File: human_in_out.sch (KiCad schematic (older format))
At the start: 47 parts

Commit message: add more buttons
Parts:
- removed R?: R, symbol Device:R
- removed SW? (x2): SW_Push_45deg, symbol Switch:SW_Push_45deg
- removed U? (x7): 74HC04, symbol 74xx:74HC04
- added C?: 100n, symbol Device:C
- added C? (x8): 330n, symbol Device:C
- added R? (x7): 10k, symbol Device:R
- added SW? (x8): SW_Push, symbol Switch:SW_Push
- added U? (x14): 74HC14, symbol 74xx:74HC14
- R?: value R -> 10k
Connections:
- net labels added: BTN3, BTN4, BTN5, BTN6, BTN7, BTN8
- wire segments 58 -> 99
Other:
- moved on the sheet: C?, R?, SW?

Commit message: Finish LED branches on programmer sheet
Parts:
- added D? (x2): LED, symbol Device:LED
- added R? (x2): R, symbol Device:R
- added U? (x2): 74HC14, symbol 74xx:74HC14
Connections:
- net +3V3: now also R?.1, R?.1
- new net: D?.1 (K), U?.8
- new net: D?.1 (K), U?.12
- new net: D?.2 (A), R?.2 (x2)
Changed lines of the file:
@@
 Wire Wire Line
 	4850 1450 6200 1450
-Wire Bus Line
-	4550 4750 4550 5900
-Wire Bus Line
-	6300 900  6300 4750
 Text Label 5950 1450 0    50   ~ 0
 BTN1
@@
 Text Label 6000 2850 0    50   ~ 0
 BTN8
+$Comp
+L Device:LED D?
+U 1 1 60ACE318
+P 8400 5250
+F 0 "D?" V 8439 5132 50  0000 R CNN
+F 1 "LED" V 8348 5132 50  0000 R CNN
+F 2 "" H 8400 5250 50  0001 C CNN
+F 3 "~" H 8400 5250 50  0001 C CNN
+	1    8400 5250
+	0    -1   -1   0
+$EndComp
+$Comp
+L Device:R R?
+U 1 1 60ACF032
+P 8400 4950
+F 0 "R?" H 8470 4996 50  0000 L CNN
+F 1 "R" H 8470 4905 50  0000 L CNN
+F 2 "" V 8330 4950 50  0001 C CNN
+F 3 "~" H 8400 4950 50  0001 C CNN
+	1    8400 4950
+	1    0    0    -1
+$EndComp
+$Comp
+L Device:LED D?
+U 1 1 60ACF03C
+P 8800 5250
+F 0 "D?" V 8839 5132 50  0000 R CNN
+F 1 "LED" V 8748 5132 50  0000 R CNN
+F 2 "" H 8800 5250 50  0001 C CNN
+F 3 "~" H 8800 5250 50  0001 C CNN
+	1    8800 5250
+	0    -1   -1   0
+$EndComp
+$Comp
+L Device:R R?
+U 1 1 60ACF046
+P 8800 4950
+F 0 "R?" H 8870 4996 50  0000 L CNN
+F 1 "R" H 8870 4905 50  0000 L CNN
+F 2 "" V 8730 4950 50  0001 C CNN
+F 3 "~" H 8800 4950 50  0001 C CNN
+	1    8800 4950
+	1    0    0    -1
+$EndComp
+$Comp
+L power:+3.3V #PWR?
+U 1 1 60ACF050
+P 8400 4800
+F 0 "#PWR?" H 8400 4650 50  0001 C CNN
+F 1 "+3.3V" H 8415 4973 50  0000 C CNN
+F 2 "" H 8400 4800 50  0001 C CNN
+F 3 "" H 8400 4800 50  0001 C CNN
+	1    8400 4800
+	1    0    0    -1
+$EndComp
+$Comp
+L power:+3.3V #PWR?
+U 1 1 60ACF05A
+P 8800 4800
+F 0 "#PWR?" H 8800 4650 50  0001 C CNN
+F 1 "+3.3V" H 8815 4973 50  0000 C CNN
+F 2 "" H 8800 4800 50  0001 C CNN
+F 3 "" H 8800 4800 50  0001 C CNN
+	1    8800 4800
+	1    0    0    -1
+$EndComp
+$Comp
+L 74xx:74HC14 U?
+U 6 1 60AC6636
+P 8000 6050
+F 0 "U?" H 8000 6367 50  0000 C CNN
+F 1 "74HC14" H 8000 6276 50  0000 C CNN
+F 2 "" H 8000 6050 50  0001 C CNN
+F 3 "http://www.ti.com/lit/gpn/sn74HC14" H 8000 6050 50  0001 C CNN
+	6    8000 6050
+	1    0    0    -1
+$EndComp
+$Comp
+L 74xx:74HC14 U?
+U 4 1 60AC6630
+P 8000 5500
+AR Path="/6005349A/60AC6630" Ref="U?"  Part="4"
+AR Path="/608DD7ED/60AC6630" Ref="U?"  Part="4"
+F 0 "U?" H 8000 5817 50  0000 C CNN
+F 1 "74HC14" H 8000 5726 50  0000 C CNN
+F 2 "" H 8000 5500 50  0001 C CNN
+F 3 "http://www.ti.com/lit/gpn/sn74HC14" H 8000 5500 50  0001 C CNN
+	4    8000 5500
+	1    0    0    -1
+$EndComp
+Wire Wire Line
+	8300 5500 8400 5500
+Wire Wire Line
+	8400 5500 8400 5400
+Wire Wire Line
+	8300 6050 8800 6050
+Wire Wire Line
+	8800 6050 8800 5400
+Wire Bus Line
+	4550 4750 4550 5900
+Wire Bus Line
+	6300 900  6300 4750
 $EndSCHEMATC

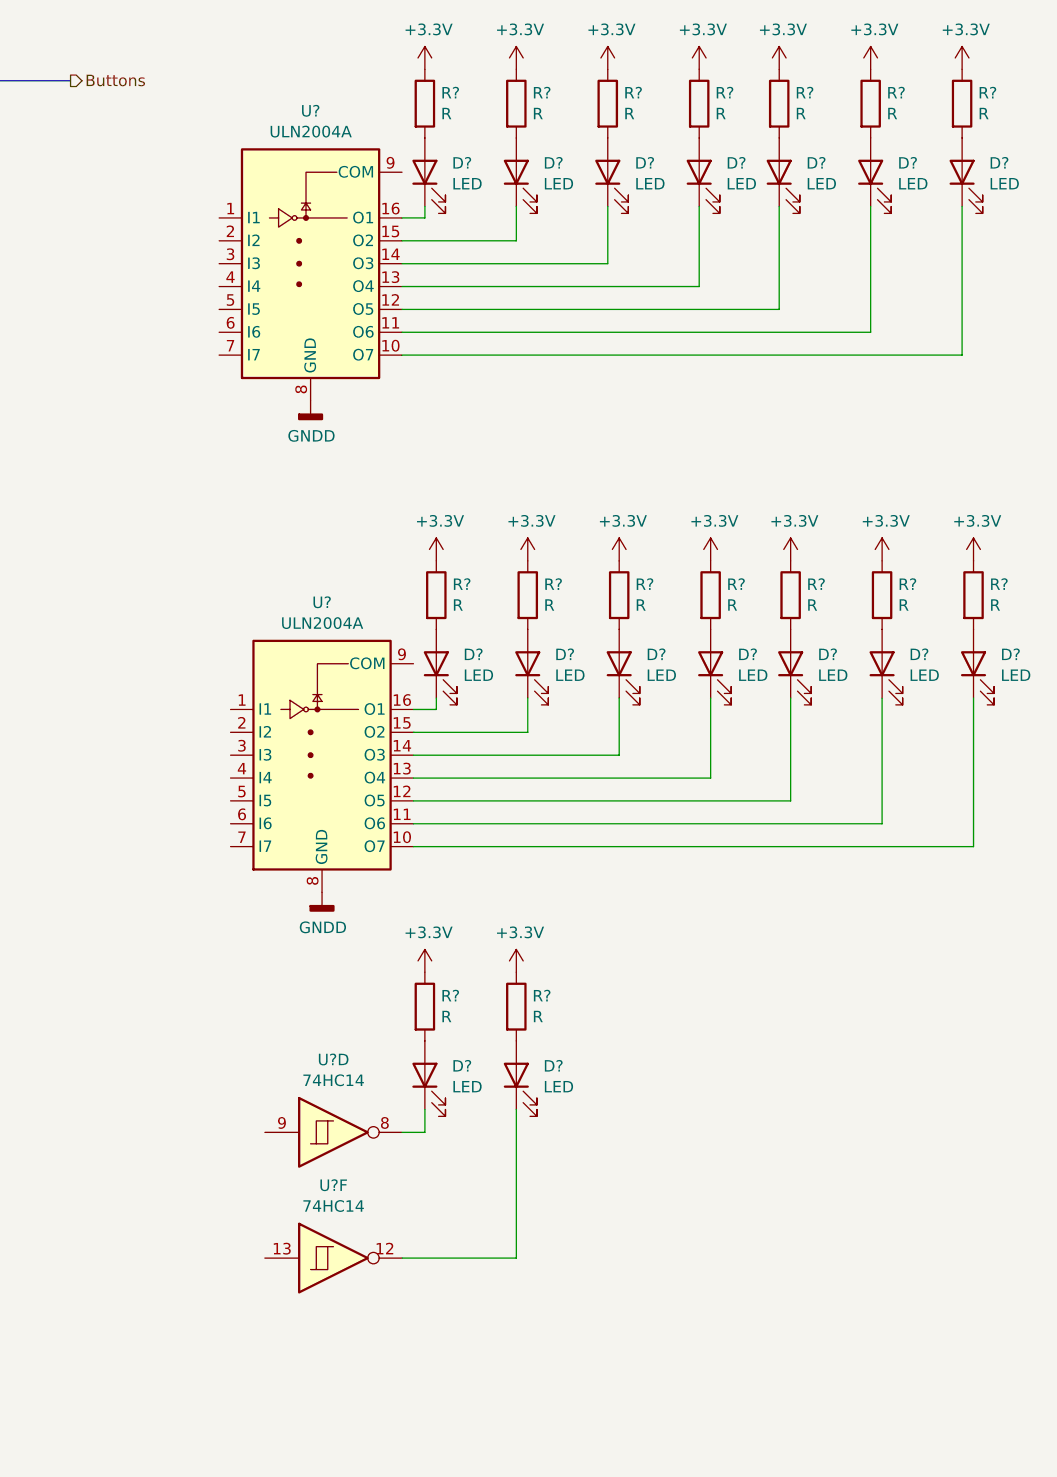
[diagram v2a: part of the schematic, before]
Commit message: connect leds to fpga
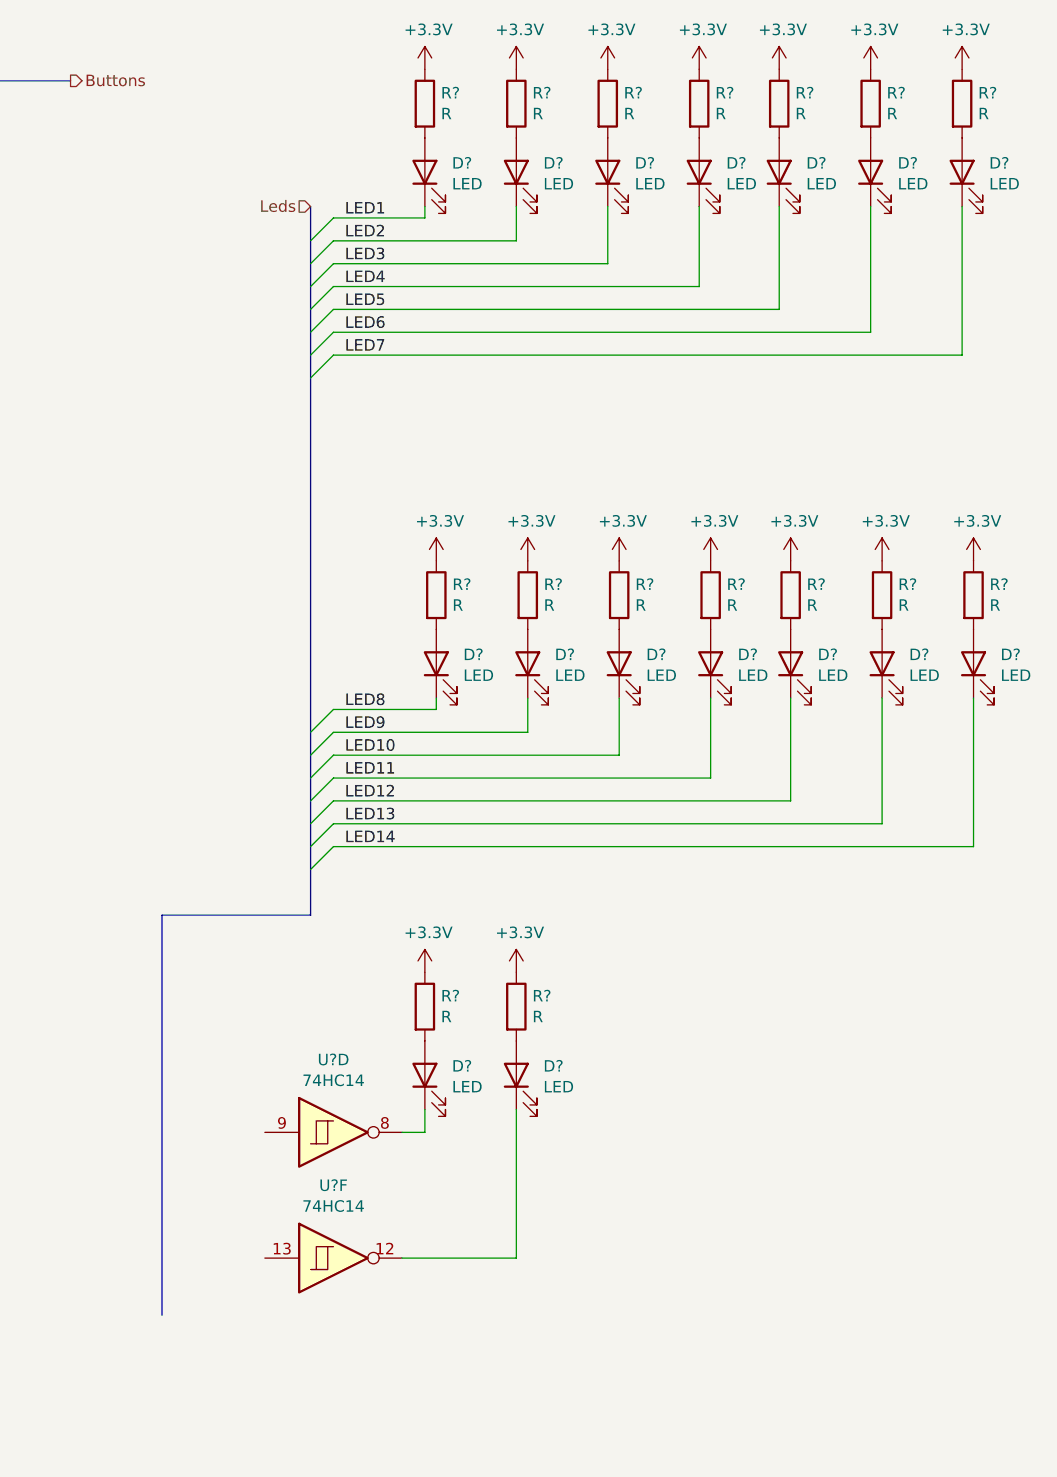
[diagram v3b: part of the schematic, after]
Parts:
- removed U? (x2): ULN2004A, symbol Transistor_Array:ULN2004A
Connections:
- net LED1: now reaches D?.1 (K)
- net LED2: now reaches D?.1 (K)
- net LED3: now reaches D?.1 (K)
- net LED4: now reaches D?.1 (K)
- net LED5: now reaches D?.1 (K)
- net LED6: now reaches D?.1 (K)
- net LED7: now reaches D?.1 (K)
- net LED8: now reaches D?.1 (K)
- net LED9: now reaches D?.1 (K)
- net LED10: now reaches D?.1 (K)
- net LED11: now reaches D?.1 (K)
- net LED12: now reaches D?.1 (K)
- net LED13: now reaches D?.1 (K)
- net LED14: now reaches D?.1 (K)
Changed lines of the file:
@@
-$EndComp
-$Comp
-L Transistor_Array:ULN2004A U?
-U 1 1 60912981
-P 7900 1700
-F 0 "U?" H 7900 2367 50  0000 C CNN
-F 1 "ULN2004A" H 7900 2276 50  0000 C CNN
-F 2 "" H 7950 1150 50  0001 L CNN
-F 3 "http://www.ti.com/lit/ds/symlink/uln2003a.pdf" H 8000 1500 50  0001 C CNN
-	1    7900 1700
-	1    0    0    -1
 $EndComp
 $Comp
@@
 $EndComp
 Wire Wire Line
-	8300 1500 8400 1500
-Wire Wire Line
 	8400 1500 8400 1450
 Wire Wire Line
-	8300 1600 8800 1600
-Wire Wire Line
 	8800 1600 8800 1450
 Wire Wire Line
-	8300 1700 9200 1700
-Wire Wire Line
 	9200 1700 9200 1450
 Wire Wire Line
-	8300 1800 9600 1800
-Wire Wire Line
 	9600 1800 9600 1450
-Wire Wire Line
-	8300 1900 9950 1900
-Wire Wire Line
-	9950 1900 9950 1450
-Wire Wire Line
-	8300 2000 10350 2000
-Wire Wire Line
-	10350 2000 10350 1450
-Wire Wire Line
-	8300 2100 10750 2100
-Wire Wire Line
-	10750 2100 10750 1450
-$Comp
-L power:GNDD #PWR?
-U 1 1 60931A66
-P 7900 2300
-F 0 "#PWR?" H 7900 2050 50  0001 C CNN
-F 1 "GNDD" H 7904 2145 50  0000 C CNN
-F 2 "" H 7900 2300 50  0001 C CNN
-F 3 "" H 7900 2300 50  0001 C CNN
-	1    7900 2300
-	1    0    0    -1
-$EndComp
 $Comp
 L Device:LED D?
@@
 $EndComp
 $Comp
-L Transistor_Array:ULN2004A U?
-U 1 1 60964128
-P 7950 3850
-F 0 "U?" H 7950 4517 50  0000 C CNN
-F 1 "ULN2004A" H 7950 4426 50  0000 C CNN
-F 2 "" H 8000 3300 50  0001 L CNN
-F 3 "http://www.ti.com/lit/ds/symlink/uln2003a.pdf" H 8050 3650 50  0001 C CNN
-	1    7950 3850
-	1    0    0    -1
-$EndComp
-$Comp
 L power:+3.3V #PWR?
 U 1 1 60964132
@@
 $EndComp
 Wire Wire Line
-	8350 3650 8450 3650
-Wire Wire Line
 	8450 3650 8450 3600
 Wire Wire Line
-	8350 3750 8850 3750
-Wire Wire Line
 	8850 3750 8850 3600
 Wire Wire Line
-	8350 3850 9250 3850
-Wire Wire Line
 	9250 3850 9250 3600
 Wire Wire Line
-	8350 3950 9650 3950
-Wire Wire Line
 	9650 3950 9650 3600
-Wire Wire Line
-	8350 4050 10000 4050
-Wire Wire Line
-	10000 4050 10000 3600
-Wire Wire Line
-	8350 4150 10400 4150
-Wire Wire Line
-	10400 4150 10400 3600
-Wire Wire Line
-	8350 4250 10800 4250
-Wire Wire Line
-	10800 4250 10800 3600
-$Comp
-L power:GNDD #PWR?
-U 1 1 60964186
-P 7950 4450
-F 0 "#PWR?" H 7950 4200 50  0001 C CNN
-F 1 "GNDD" H 7954 4295 50  0000 C CNN
-F 2 "" H 7950 4450 50  0001 C CNN
-F 3 "" H 7950 4450 50  0001 C CNN
-	1    7950 4450
-	1    0    0    -1
-$EndComp
 $Comp
 L Device:R R?
@@
 Wire Wire Line
 	8800 6050 8800 5400
+Wire Wire Line
+	8000 1500 8400 1500
+Entry Wire Line
+	7900 1600 8000 1500
+Wire Wire Line
+	8000 1600 8800 1600
+Wire Wire Line
+	8000 1700 9200 1700
+Wire Wire Line
+	8000 1800 9600 1800
+Wire Wire Line
+	8000 1900 9950 1900
+Wire Wire Line
+	8000 2000 10350 2000
+Wire Wire Line
+	8000 2100 10750 2100
+Entry Wire Line
+	7900 1700 8000 1600
+Entry Wire Line
+	7900 1900 8000 1800
+Entry Wire Line
+	7900 1800 8000 1700
+Entry Wire Line
+	7900 2000 8000 1900
+Entry Wire Line
+	7900 2100 8000 2000
+Entry Wire Line
+	7900 2200 8000 2100
+Entry Wire Line
+	7900 3750 8000 3650
+Entry Wire Line
+	7900 3850 8000 3750
+Entry Wire Line
+	7900 4050 8000 3950
+Entry Wire Line
+	7900 3950 8000 3850
+Entry Wire Line
+	7900 4150 8000 4050
+Entry Wire Line
+	7900 4250 8000 4150
+Entry Wire Line
+	7900 4350 8000 4250
+Wire Wire Line
+	8000 3650 8450 3650
+Wire Wire Line
+	8000 3750 8850 3750
+Wire Wire Line
+	8000 3850 9250 3850
+Wire Wire Line
+	8000 3950 9650 3950
+Wire Wire Line
+	8000 4050 10000 4050
+Wire Wire Line
+	8000 4150 10400 4150
+Wire Wire Line
+	8000 4250 10800 4250
+Text Label 8050 1500 0    50   ~ 0
+LED1
+Text Label 8050 1600 0    50   ~ 0
+LED2
+Text Label 8050 1700 0    50   ~ 0
+LED3
+Text Label 8050 1800 0    50   ~ 0
+LED4
+Text Label 8050 1900 0    50   ~ 0
+LED5
+Text Label 8050 2000 0    50   ~ 0
+LED6
+Text Label 8050 2100 0    50   ~ 0
+LED7
+Text Label 8050 3650 0    50   ~ 0
+LED8
+Text Label 8050 3750 0    50   ~ 0
+LED9
+Text Label 8050 3850 0    50   ~ 0
+LED10
+Text Label 8050 3950 0    50   ~ 0
+LED11
+Text Label 8050 4050 0    50   ~ 0
+LED12
+Text Label 8050 4150 0    50   ~ 0
+LED13
+Text Label 8050 4250 0    50   ~ 0
+LED14
+Wire Wire Line
+	10000 3600 10000 4050
+Wire Wire Line
+	10400 3600 10400 4150
+Wire Wire Line
+	10800 3600 10800 4250
+Wire Wire Line
+	9950 1450 9950 1900
+Wire Wire Line
+	10350 1450 10350 2000
+Wire Wire Line
+	10750 1450 10750 2100
+Text HLabel 7900 1450 0    50   Input ~ 0
+Leds
+Wire Bus Line
+	7900 4550 7250 4550
+Wire Bus Line
+	7250 4550 7250 6300
 Wire Bus Line
 	4550 4750 4550 5900
 Wire Bus Line
 	6300 900  6300 4750
+Wire Bus Line
+	7900 1450 7900 4550
 $EndSCHEMATC

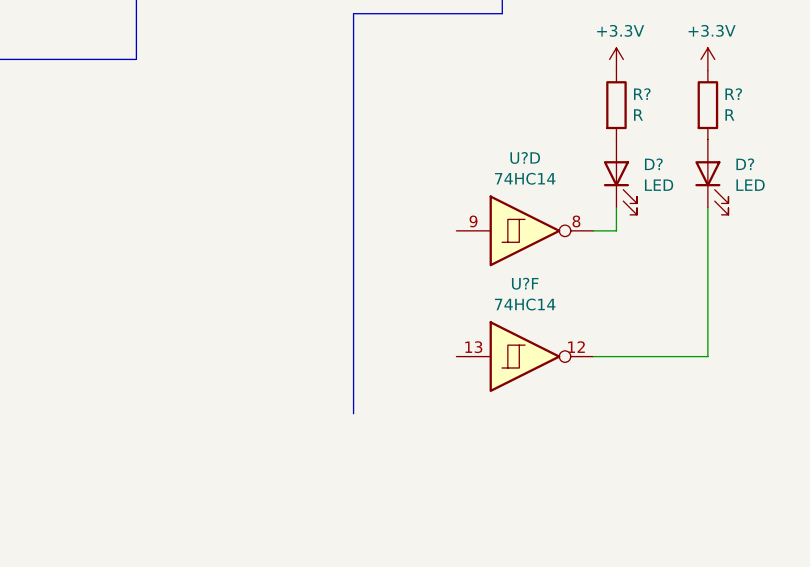
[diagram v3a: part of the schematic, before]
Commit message: plus 2 leds
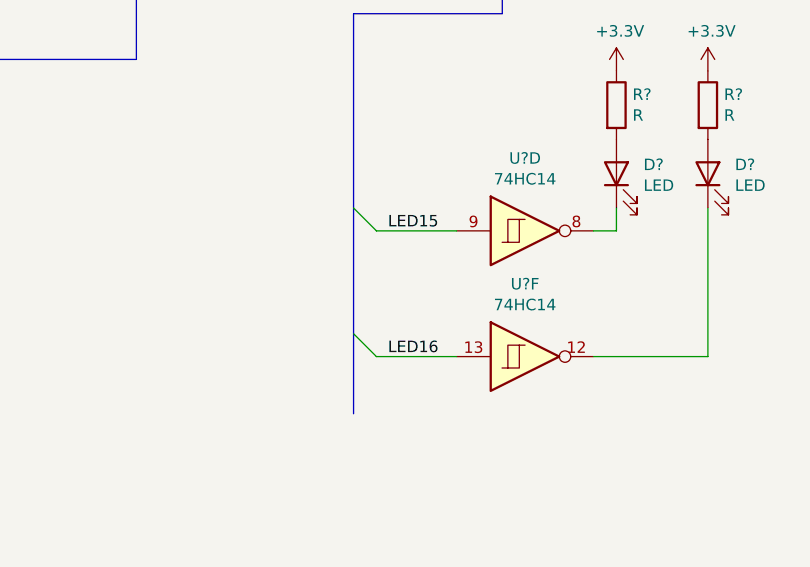
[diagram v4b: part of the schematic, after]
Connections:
- net LED15: now reaches U?.9
- net LED16: now reaches U?.13
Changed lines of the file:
@@
 Wire Bus Line
 	7900 4550 7250 4550
+Entry Wire Line
+	7250 5950 7350 6050
+Entry Wire Line
+	7250 5400 7350 5500
+Wire Wire Line
+	7350 5500 7700 5500
+Wire Wire Line
+	7350 6050 7700 6050
 Wire Bus Line
 	7250 4550 7250 6300
@@
 Wire Bus Line
 	7900 1450 7900 4550
+Text Label 7400 5500 0    50   ~ 0
+LED15
+Text Label 7400 6050 0    50   ~ 0
+LED16
 $EndSCHEMATC

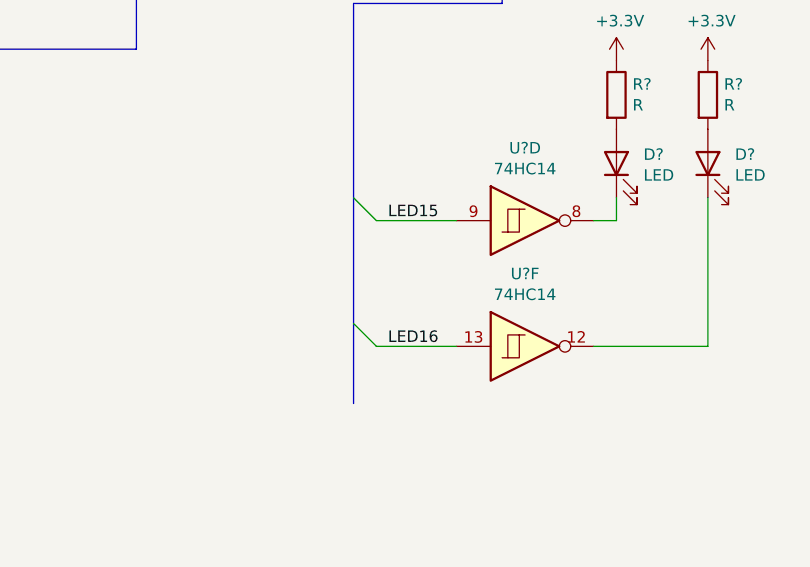
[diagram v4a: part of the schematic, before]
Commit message: Add LED15 and LED16
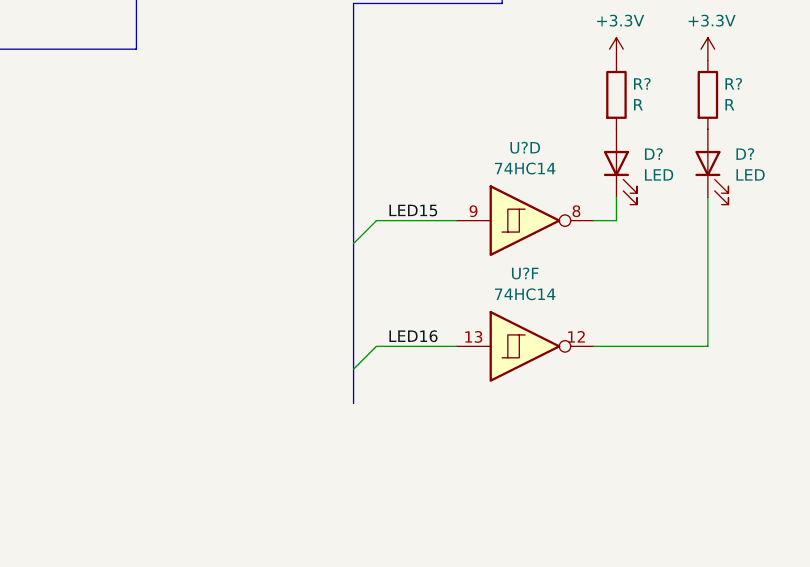
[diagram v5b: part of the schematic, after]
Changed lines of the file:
@@
 	7900 4550 7250 4550
 Entry Wire Line
-	7250 5950 7350 6050
+	7250 5600 7350 5500
 Entry Wire Line
-	7250 5400 7350 5500
+	7250 6150 7350 6050
 Wire Wire Line
-	7350 5500 7700 5500
+	7700 5500 7350 5500
 Wire Wire Line
 	7350 6050 7700 6050
+Text Label 7400 5500 0    50   ~ 0
+LED15
+Text Label 7400 6050 0    50   ~ 0
+LED16
 Wire Bus Line
 	7250 4550 7250 6300
@@
 Wire Bus Line
 	7900 1450 7900 4550
-Text Label 7400 5500 0    50   ~ 0
-LED15
-Text Label 7400 6050 0    50   ~ 0
-LED16
 $EndSCHEMATC
